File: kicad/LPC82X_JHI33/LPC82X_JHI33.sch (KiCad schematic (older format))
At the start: 2 parts

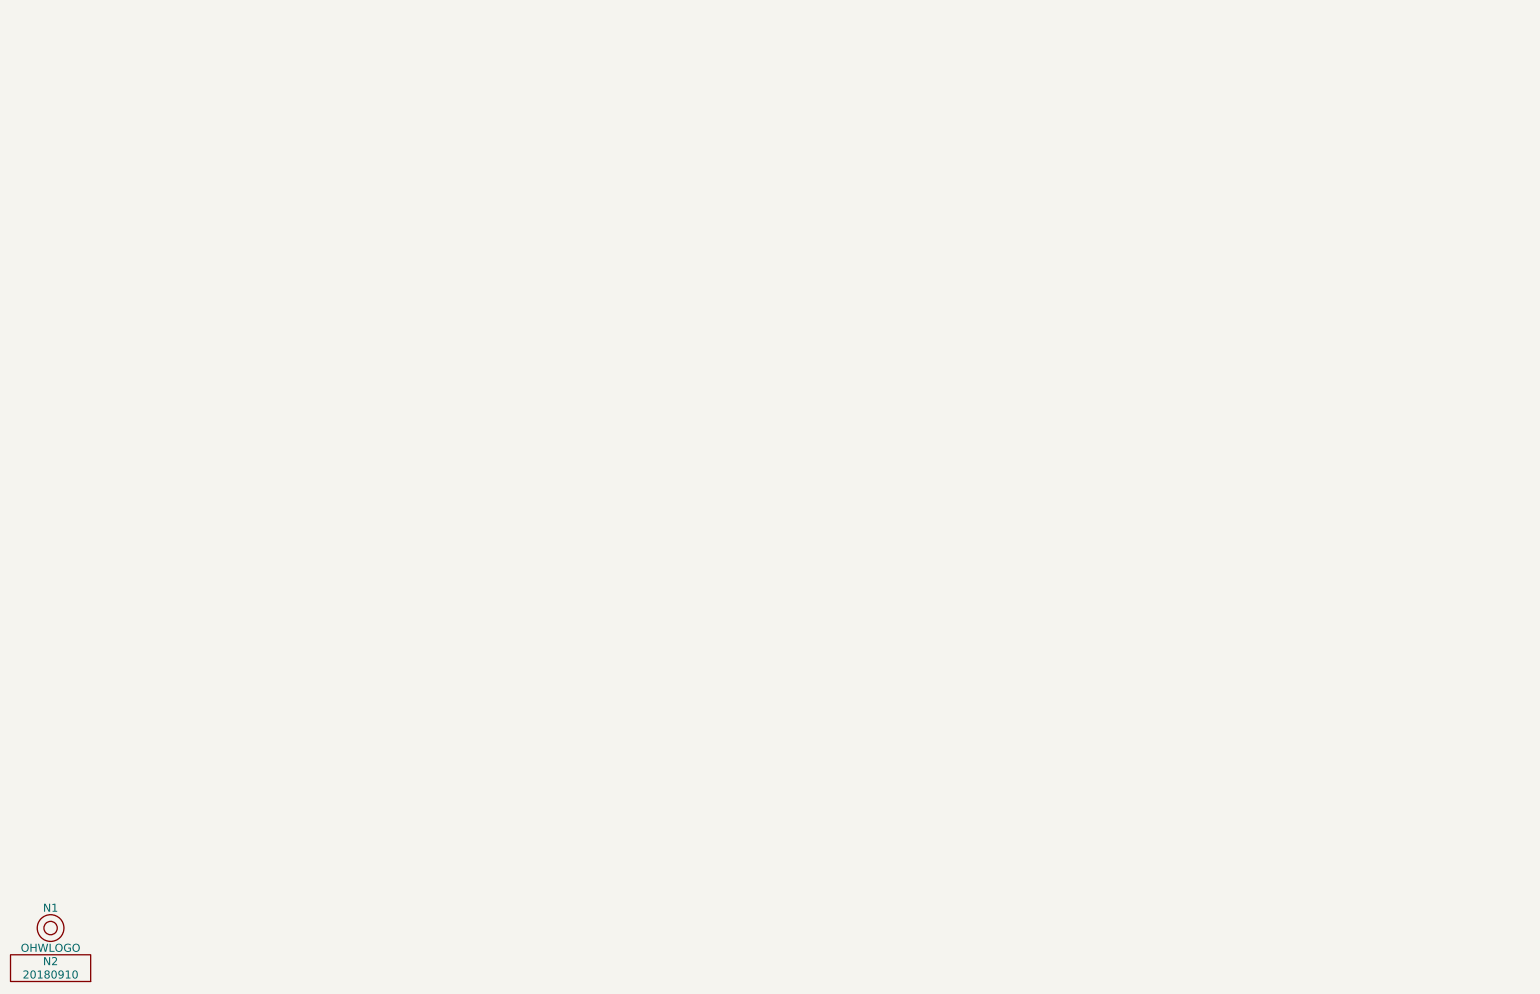
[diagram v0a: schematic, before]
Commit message: started on LPC824 QFN33 breakout
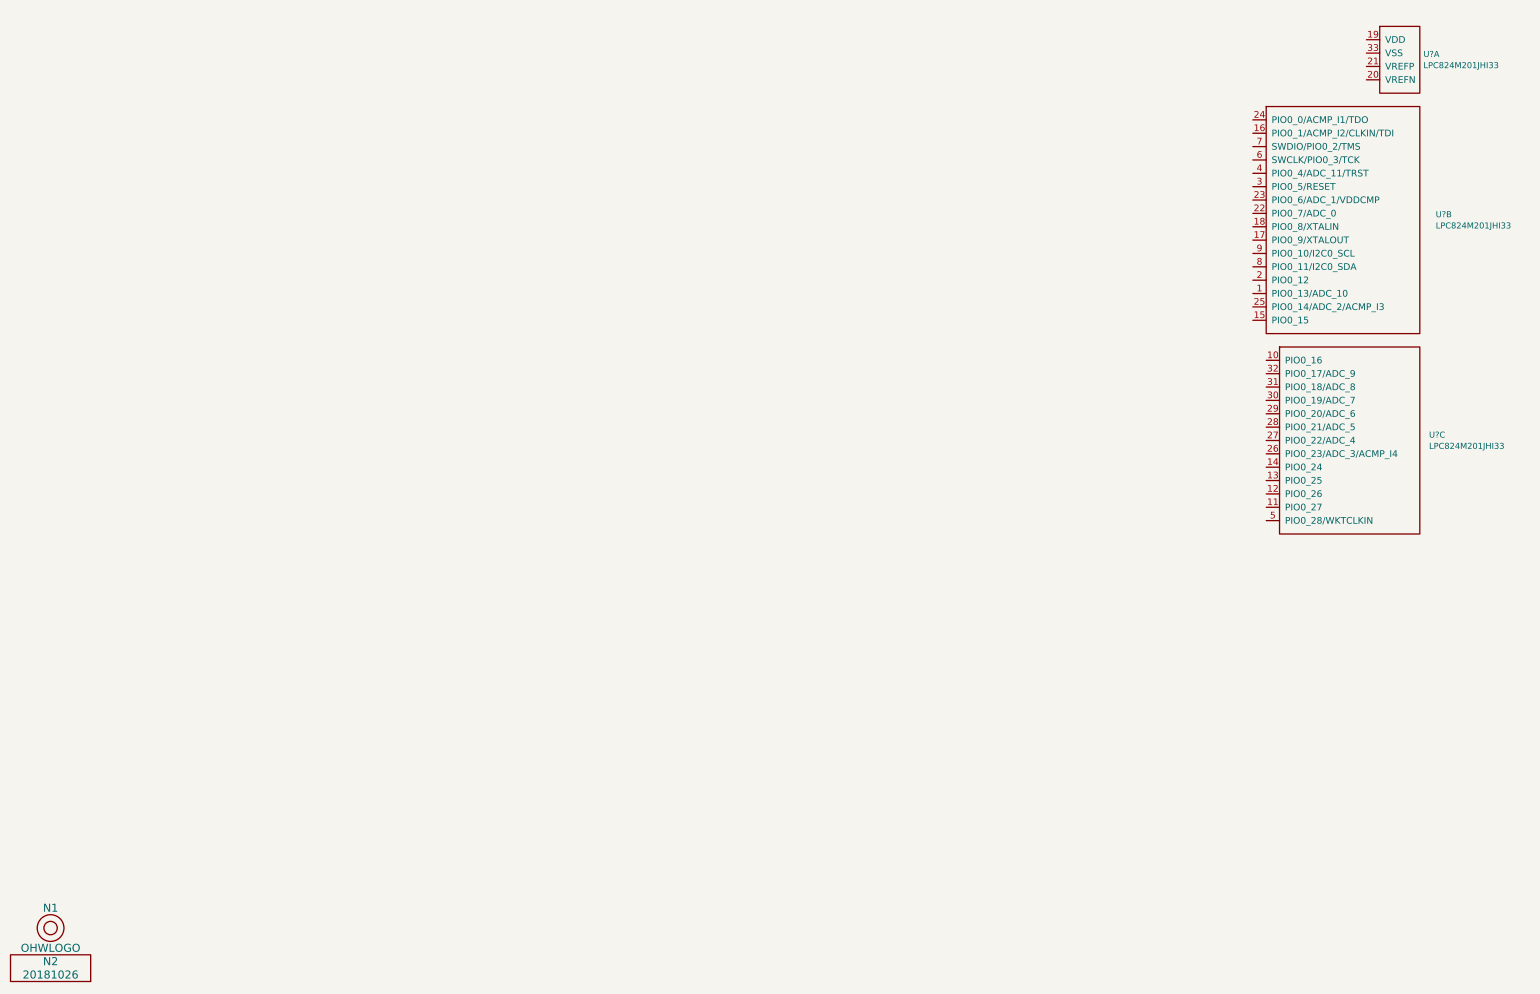
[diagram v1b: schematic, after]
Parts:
- added U? (x3): LPC824M201JHI33, SquantorNxp_SOT617-3, symbol SquantorNxp:LPC824M201JHI33
- N2: value 20180910 -> 20181026
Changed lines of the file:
@@
 EESchema Schematic File Version 4
-LIBS:OSH_Park_2_layer-cache
+LIBS:LPC82X_JHI33-cache
 EELAYER 26 0
 EELAYER END
@@
 P 850 7700
 F 0 "N2" H 850 7800 60  0000 C CNN
-F 1 "20180910" H 850 7700 60  0000 C CNN
+F 1 "20181026" H 850 7700 60  0000 C CNN
 F 2 "SquantorLabels:Label_version" H 850 7700 60  0001 C CNN
 F 3 "" H 850 7700 60  0001 C CNN
@@
 	1    0    0    -1
 $EndComp
+$Comp
+L SquantorNxp:LPC824M201JHI33 U?
+U 1 1 5BD2C0FE
+P 10950 850
+F 0 "U?" H 11127 892 45  0000 L CNN
+F 1 "LPC824M201JHI33" H 11127 808 45  0000 L CNN
+F 2 "SquantorNxp_SOT617-3" H 11500 -50 20  0001 C CNN
+F 3 "" H 10300 750 60  0000 C CNN
+	1    10950 850
+	1    0    0    -1
+$EndComp
+$Comp
+L SquantorNxp:LPC824M201JHI33 U?
+U 2 1 5BD2C2D1
+P 10500 2050
+F 0 "U?" H 11219 2092 45  0000 L CNN
+F 1 "LPC824M201JHI33" H 11219 2008 45  0000 L CNN
+F 2 "SquantorNxp_SOT617-3" H 11050 1150 20  0001 C CNN
+F 3 "" H 9850 1950 60  0000 C CNN
+	2    10500 2050
+	1    0    0    -1
+$EndComp
+$Comp
+L SquantorNxp:LPC824M201JHI33 U?
+U 3 1 5BD2C34E
+P 10550 3700
+F 0 "U?" H 11169 3742 45  0000 L CNN
+F 1 "LPC824M201JHI33" H 11169 3658 45  0000 L CNN
+F 2 "SquantorNxp_SOT617-3" H 11100 2800 20  0001 C CNN
+F 3 "" H 9900 3600 60  0000 C CNN
+	3    10550 3700
+	1    0    0    -1
+$EndComp

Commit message: started with schematic entry of QFN33 LPC824 breakout
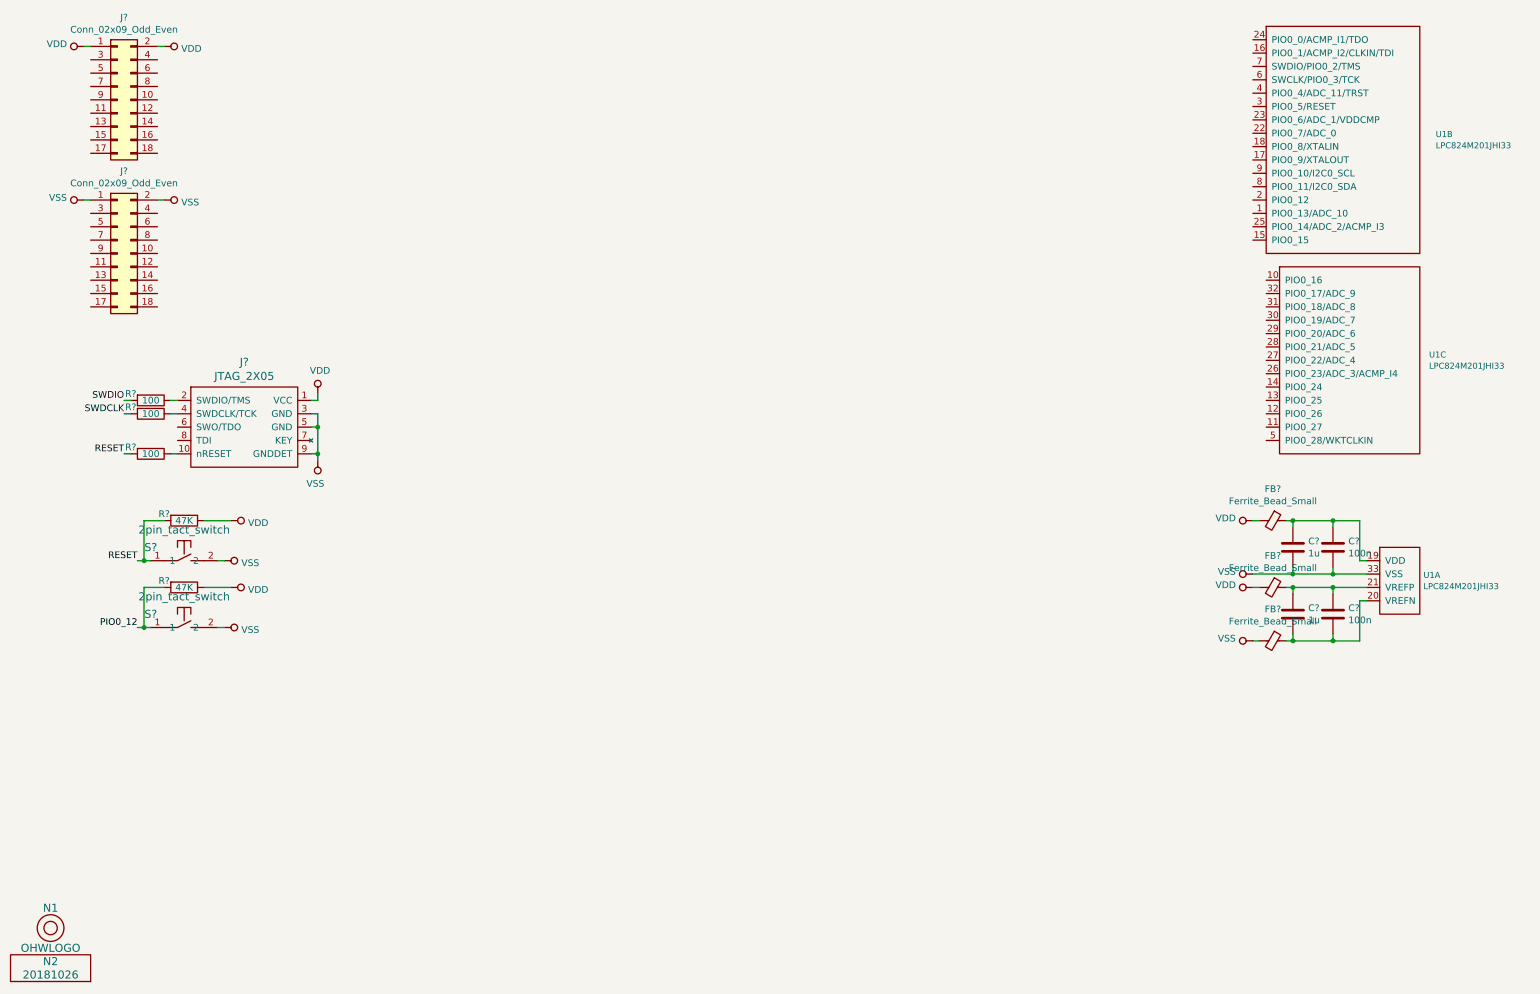
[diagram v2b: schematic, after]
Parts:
- added C? (x2): 100n, SquantorRcl:C_0402, symbol Device:C
- added C? (x2): 1u, SquantorRcl:C_0805, symbol Device:C
- added FB? (x3): Ferrite_Bead_Small, SquantorRcl:C_0402, symbol Device:Ferrite_Bead_Small
- added J? (x2): Conn_02x09_Odd_Even, SquantorConnectors:Header-0254-2X09-H010, symbol Connector_Generic:Conn_02x09_Odd_Even
- added J?: JTAG_2X05, symbol SquantorConnectors:JTAG_2X05
- added R? (x3): 100, SquantorRcl:R_0402_hand, symbol Device:R
- added R? (x2): 47K, SquantorRcl:R_0402_hand, symbol Device:R
- added S? (x2): 2pin_tact_switch, symbol SquantorButtons:2pin_tact_switch
- U1: renamed from U?; footprint SquantorNxp_SOT617-3 -> SquantorIC:SOT617-3
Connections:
- net at U1.19 (VDD): now also C?.1, C?.1, FB?.1
- net at U1.20 (VREFN): now also C?.2, C?.2, FB?.1
- net at U1.21 (VREFP): now also C?.1, C?.1, FB?.1
- net VSS: now reaches U1.33 (VSS)
- net VSS: now also C?.2, C?.2, FB?.2, J?.1 (Pin_1), J?.2 (Pin_2), J?.3 (GND), J?.5 (GND), J?.9 (GNDDET), S?.2, S?.2
- new net: J?.10 (nRESET), R?.1
- new net: J?.2 (SWDIO/TMS), R?.1
- new net: J?.4 (SWDCLK/TCK), R?.1
- new net PIO0_12: R?.2, S?.1
- new net RESET: R?.2, R?.2, S?.1
- new net SWDCLK: R?.2
- new net SWDIO: R?.2
- new net VDD: FB?.2, FB?.2, J?.1 (Pin_1), J?.1 (VCC), J?.2 (Pin_2), R?.1, R?.1
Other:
- moved on the sheet: U1A, U1B, U1C

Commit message: more schematic updates updated footprint of a used button
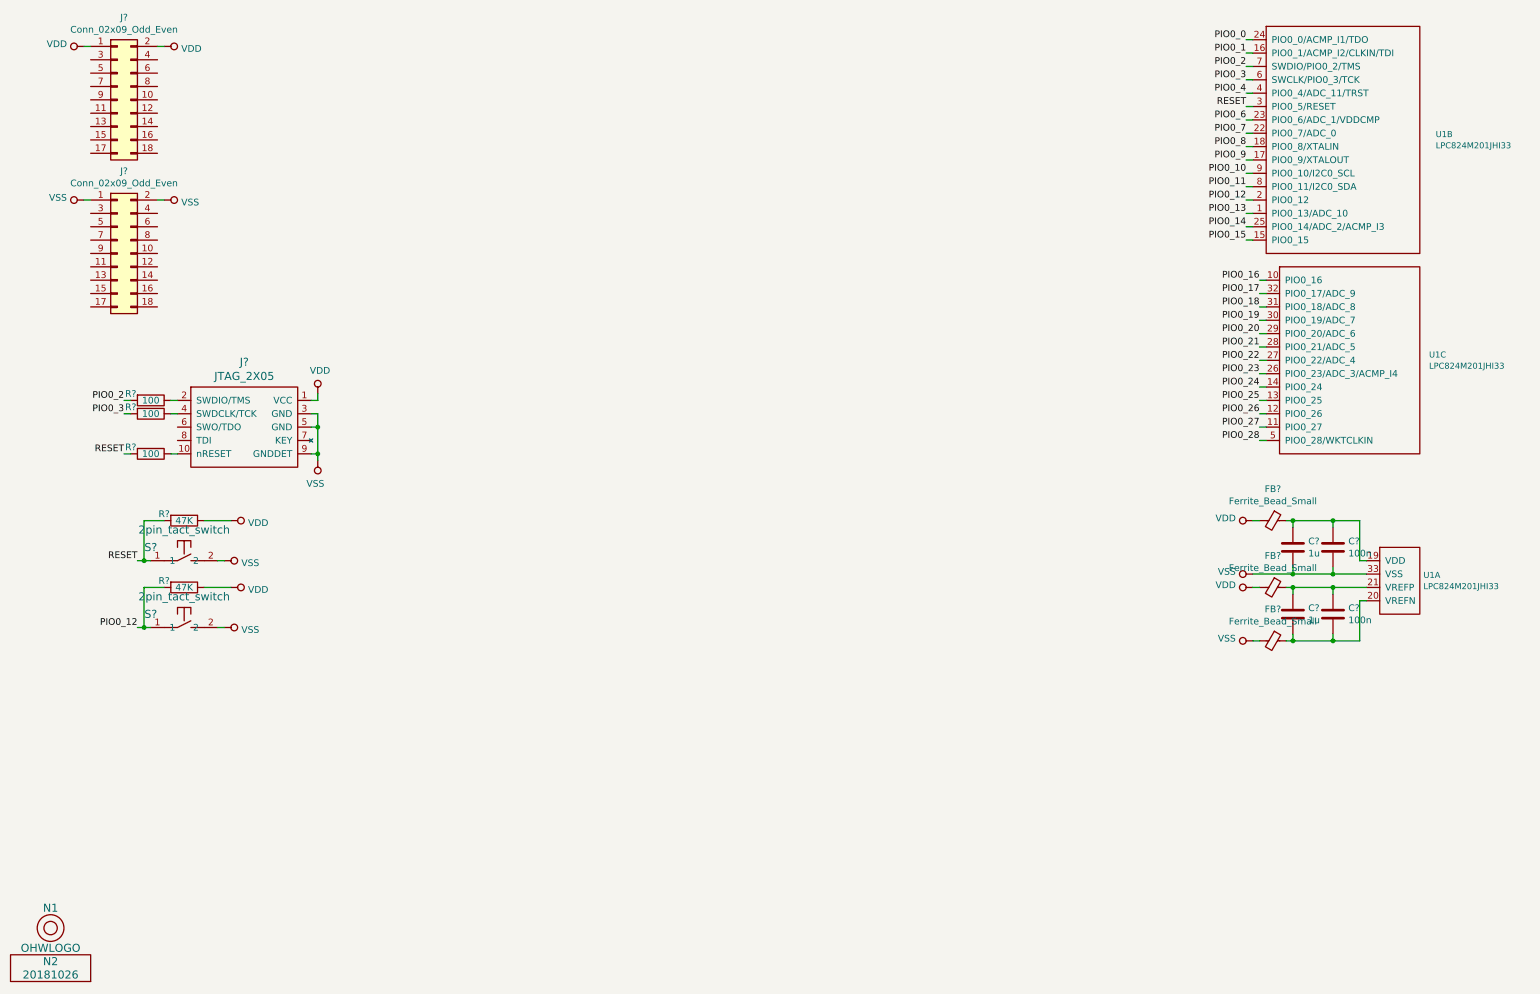
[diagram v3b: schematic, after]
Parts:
- S? (x2): footprint (none) -> SquantorButtons:TD-85XU
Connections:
- net SWDCLK is gone; now on net PIO0_3: R?.2
- net SWDIO is gone; now on net PIO0_2: R?.2
- net PIO0_12: now also U1.2 (PIO0_12)
- net RESET: now also U1.3 (PIO0_5/RESET)
- net PIO0_13: now reaches U1.1 (PIO0_13/ADC_10)
- net PIO0_15: now reaches U1.15 (PIO0_15)
- net PIO0_1: now reaches U1.16 (PIO0_1/ACMP_I2/CLKIN/TDI)
- net PIO0_9: now reaches U1.17 (PIO0_9/XTALOUT)
- net PIO0_8: now reaches U1.18 (PIO0_8/XTALIN)
- net PIO0_7: now reaches U1.22 (PIO0_7/ADC_0)
- net PIO0_6: now reaches U1.23 (PIO0_6/ADC_1/VDDCMP)
- net PIO0_0: now reaches U1.24 (PIO0_0/ACMP_I1/TDO)
- net PIO0_14: now reaches U1.25 (PIO0_14/ADC_2/ACMP_I3)
- net PIO0_4: now reaches U1.4 (PIO0_4/ADC_11/TRST)
- net PIO0_3: now reaches U1.6 (SWCLK/PIO0_3/TCK)
- net PIO0_2: now reaches U1.7 (SWDIO/PIO0_2/TMS)
- net PIO0_11: now reaches U1.8 (PIO0_11/I2C0_SDA)
- net PIO0_10: now reaches U1.9 (PIO0_10/I2C0_SCL)
- net PIO0_16: now reaches U1.10 (PIO0_16)
- net PIO0_27: now reaches U1.11 (PIO0_27)
- net PIO0_26: now reaches U1.12 (PIO0_26)
- net PIO0_25: now reaches U1.13 (PIO0_25)
- net PIO0_24: now reaches U1.14 (PIO0_24)
- net PIO0_23: now reaches U1.26 (PIO0_23/ADC_3/ACMP_I4)
- net PIO0_22: now reaches U1.27 (PIO0_22/ADC_4)
- net PIO0_21: now reaches U1.28 (PIO0_21/ADC_5)
- net PIO0_20: now reaches U1.29 (PIO0_20/ADC_6)
- net PIO0_19: now reaches U1.30 (PIO0_19/ADC_7)
- net PIO0_18: now reaches U1.31 (PIO0_18/ADC_8)
- net PIO0_17: now reaches U1.32 (PIO0_17/ADC_9)
- net PIO0_28: now reaches U1.5 (PIO0_28/WKTCLKIN)
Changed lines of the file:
@@
 	1450 3400 1400 3400
 Text Label 1400 3400 2    50   ~ 0
-SWDIO
+PIO0_2
 Text Label 1400 3500 2    50   ~ 0
-SWDCLK
+PIO0_3
 $Comp
 L Device:R R?
@@
 F 0 "S?" H 1600 4700 60  0000 C CNN
 F 1 "2pin_tact_switch" H 1850 4831 60  0000 C CNN
-F 2 "" H 1850 4600 60  0001 C CNN
+F 2 "SquantorButtons:TD-85XU" H 1850 4600 60  0001 C CNN
 F 3 "" H 1850 4600 60  0001 C CNN
 	1    1850 4600
@@
 F 0 "S?" H 1600 5200 60  0000 C CNN
 F 1 "2pin_tact_switch" H 1850 5331 60  0000 C CNN
-F 2 "" H 1850 5100 60  0001 C CNN
+F 2 "SquantorButtons:TD-85XU" H 1850 5100 60  0001 C CNN
 F 3 "" H 1850 5100 60  0001 C CNN
 	1    1850 5100
@@
 Text Label 1500 5100 2    50   ~ 0
 PIO0_12
+Text Label 9800 1200 2    50   ~ 0
+RESET
+Wire Wire Line
+	9850 1200 9800 1200
+Wire Wire Line
+	9850 1000 9800 1000
+Wire Wire Line
+	9850 900  9800 900
+Text Label 9800 1900 2    50   ~ 0
+PIO0_12
+Wire Wire Line
+	9850 1900 9800 1900
+Wire Wire Line
+	9850 700  9800 700
+Wire Wire Line
+	9850 800  9800 800
+Wire Wire Line
+	9850 1100 9800 1100
+Wire Wire Line
+	9850 1300 9800 1300
+Wire Wire Line
+	9850 1400 9800 1400
+Wire Wire Line
+	9850 1500 9800 1500
+Wire Wire Line
+	9800 1600 9850 1600
+Wire Wire Line
+	9850 1700 9800 1700
+Wire Wire Line
+	9850 1800 9800 1800
+Wire Wire Line
+	9850 2000 9800 2000
+Wire Wire Line
+	9850 2100 9800 2100
+Wire Wire Line
+	9850 2200 9800 2200
+Wire Wire Line
+	9950 2500 9900 2500
+Wire Wire Line
+	9950 2600 9900 2600
+Wire Wire Line
+	9950 2700 9900 2700
+Wire Wire Line
+	9950 2800 9900 2800
+Wire Wire Line
+	9950 2900 9900 2900
+Wire Wire Line
+	9950 3000 9900 3000
+Wire Wire Line
+	9950 3100 9900 3100
+Wire Wire Line
+	9950 3200 9900 3200
+Wire Wire Line
+	9950 3300 9900 3300
+Wire Wire Line
+	9950 3400 9900 3400
+Wire Wire Line
+	9950 3500 9900 3500
+Wire Wire Line
+	9950 3600 9900 3600
+Wire Wire Line
+	9950 3700 9900 3700
+Text Label 9800 700  2    50   ~ 0
+PIO0_0
+Text Label 9800 800  2    50   ~ 0
+PIO0_1
+Text Label 9800 1100 2    50   ~ 0
+PIO0_4
+Text Label 9800 900  2    50   ~ 0
+PIO0_2
+Text Label 9800 1000 2    50   ~ 0
+PIO0_3
+Text Label 9800 1300 2    50   ~ 0
+PIO0_6
+Text Label 9800 1400 2    50   ~ 0
+PIO0_7
+Text Label 9800 1500 2    50   ~ 0
+PIO0_8
+Text Label 9800 1600 2    50   ~ 0
+PIO0_9
+Text Label 9800 1700 2    50   ~ 0
+PIO0_10
+Text Label 9800 1800 2    50   ~ 0
+PIO0_11
+Text Label 9800 2000 2    50   ~ 0
+PIO0_13
+Text Label 9800 2100 2    50   ~ 0
+PIO0_14
+Text Label 9800 2200 2    50   ~ 0
+PIO0_15
+Text Label 9900 2500 2    50   ~ 0
+PIO0_16
+Text Label 9900 2600 2    50   ~ 0
+PIO0_17
+Text Label 9900 2700 2    50   ~ 0
+PIO0_18
+Text Label 9900 2800 2    50   ~ 0
+PIO0_19
+Text Label 9900 2900 2    50   ~ 0
+PIO0_20
+Text Label 9900 3000 2    50   ~ 0
+PIO0_21
+Text Label 9900 3100 2    50   ~ 0
+PIO0_22
+Text Label 9900 3200 2    50   ~ 0
+PIO0_23
+Text Label 9900 3300 2    50   ~ 0
+PIO0_24
+Text Label 9900 3400 2    50   ~ 0
+PIO0_25
+Text Label 9900 3500 2    50   ~ 0
+PIO0_26
+Text Label 9900 3600 2    50   ~ 0
+PIO0_27
+Text Label 9900 3700 2    50   ~ 0
+PIO0_28
 $EndSCHEMATC
